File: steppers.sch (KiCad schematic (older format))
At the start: 24 parts, among them J1 HEADER, J10 STEPSTICK, J11 STEPSTICK, J12 STEPSTICK, J2 HEADER, J3 HEADER, J4 STEPSTICK, J5 STEPSTICK, J6 STEPSTICK, J7 HEADER, J8 HEADER, J9 HEADER, P10 CONN_01X04, P11 CONN_01X04, P12 CONN_01X04, P7 CONN_02X04, P8 CONN_01X04, P9 CONN_01X04

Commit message: - added wifi esp8266 - switched caps to smd - fixed dual transistor pinout bug
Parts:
- C12, C13, C14, C15, C16, C17: footprint capacitors:ELCO-8mm-3.5mm_pitch -> capacitors:c_elec_6.3x7.7
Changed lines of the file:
@@
 EESchema Schematic File Version 2
+LIBS:rados-rescue
+LIBS:import-transistors
+LIBS:import-regulators
+LIBS:import-opamps
+LIBS:import-diodes
 LIBS:led_reverse
 LIBS:arduino_shieldsNCL
 LIBS:otheruse_transistors
 LIBS:custom_power
-LIBS:import_resistors
-LIBS:import_regulators
-LIBS:import_transistors
-LIBS:import_diodes
+LIBS:import-misc
+LIBS:armin_misc
 LIBS:power
 LIBS:device
 LIBS:transistors
 LIBS:conn
-LIBS:import_misc
 LIBS:linear
 LIBS:regul
@@
 LIBS:valves
 LIBS:arduino
+LIBS:ESP8266
 LIBS:rados-cache
 EELAYER 25 0
@@
 F 0 "C13" H 3888 1471 50  0000 L CNN
 F 1 "100uF" H 3888 1379 50  0000 L CNN
-F 2 "capacitors:ELCO-8mm-3.5mm_pitch" H 3800 1425 50  0001 C CNN
+F 2 "capacitors:c_elec_6.3x7.7" H 3800 1425 50  0001 C CNN
 F 3 "" H 3800 1425 50  0000 C CNN
 	1    3800 1425
@@
 $EndComp
 $Comp
-L Vsupply #P053
+L Vsupply #P9
 U 1 1 568BEEB3
 P 3150 775
-F 0 "#P053" H 3150 775 60  0001 C CNN
+F 0 "#P9" H 3150 775 60  0001 C CNN
 F 1 "Vsupply" H 3150 725 34  0000 C CNN
 F 2 "" H 3150 775 60  0000 C CNN
@@
 	1150 1125 1150 1425
 $Comp
-L +3.3V #PWR054
+L +3.3V #PWR2
 U 1 1 568BF4F0
 P 1150 1125
-F 0 "#PWR054" H 1150 975 50  0001 C CNN
+F 0 "#PWR2" H 1150 975 50  0001 C CNN
 F 1 "+3.3V" H 1168 1299 50  0000 C CNN
 F 2 "" H 1150 1125 50  0000 C CNN
@@
 $EndComp
 $Comp
-L +3.3V #PWR055
+L +3.3V #PWR29
 U 1 1 568BFD7B
 P 3050 1725
-F 0 "#PWR055" H 3050 1575 50  0001 C CNN
+F 0 "#PWR29" H 3050 1575 50  0001 C CNN
 F 1 "+3.3V" H 3050 1850 50  0000 C CNN
 F 2 "" H 3050 1725 50  0000 C CNN
@@
 	2900 1725 3050 1725
 $Comp
-L GND #PWR056
+L GND #PWR26
 U 1 1 568BFE54
 P 2975 1225
-F 0 "#PWR056" H 2975 975 50  0001 C CNN
+F 0 "#PWR26" H 2975 975 50  0001 C CNN
 F 1 "GND" H 2983 1051 50  0000 C CNN
 F 2 "" H 2975 1225 50  0000 C CNN
@@
 $EndComp
 $Comp
-L GND #PWR057
+L GND #PWR35
 U 1 1 568BFE70
 P 3225 1825
-F 0 "#PWR057" H 3225 1575 50  0001 C CNN
+F 0 "#PWR35" H 3225 1575 50  0001 C CNN
 F 1 "GND" H 3233 1651 50  0000 C CNN
 F 2 "" H 3225 1825 50  0000 C CNN
@@
 F 0 "C14" H 3888 2696 50  0000 L CNN
 F 1 "100uF" H 3888 2604 50  0000 L CNN
-F 2 "capacitors:ELCO-8mm-3.5mm_pitch" H 3800 2650 50  0001 C CNN
+F 2 "capacitors:c_elec_6.3x7.7" H 3800 2650 50  0001 C CNN
 F 3 "" H 3800 2650 50  0000 C CNN
 	1    3800 2650
@@
 $EndComp
 $Comp
-L Vsupply #P058
+L Vsupply #P10
 U 1 1 568BD851
 P 3150 2000
-F 0 "#P058" H 3150 2000 60  0001 C CNN
+F 0 "#P10" H 3150 2000 60  0001 C CNN
 F 1 "Vsupply" H 3150 1950 34  0000 C CNN
 F 2 "" H 3150 2000 60  0000 C CNN
@@
 	1150 2375 1150 2650
 $Comp
-L +3.3V #PWR059
+L +3.3V #PWR3
 U 1 1 568BD862
 P 1150 2375
-F 0 "#PWR059" H 1150 2225 50  0001 C CNN
+F 0 "#PWR3" H 1150 2225 50  0001 C CNN
 F 1 "+3.3V" H 1168 2549 50  0000 C CNN
 F 2 "" H 1150 2375 50  0000 C CNN
@@
 $EndComp
 $Comp
-L +3.3V #PWR060
+L +3.3V #PWR30
 U 1 1 568BD86E
 P 3050 2950
-F 0 "#PWR060" H 3050 2800 50  0001 C CNN
+F 0 "#PWR30" H 3050 2800 50  0001 C CNN
 F 1 "+3.3V" H 3050 3075 50  0000 C CNN
 F 2 "" H 3050 2950 50  0000 C CNN
@@
 	2900 2950 3050 2950
 $Comp
-L GND #PWR061
+L GND #PWR27
 U 1 1 568BD875
 P 2975 2450
-F 0 "#PWR061" H 2975 2200 50  0001 C CNN
+F 0 "#PWR27" H 2975 2200 50  0001 C CNN
 F 1 "GND" H 2983 2276 50  0000 C CNN
 F 2 "" H 2975 2450 50  0000 C CNN
@@
 $EndComp
 $Comp
-L GND #PWR062
+L GND #PWR36
 U 1 1 568BD87B
 P 3225 3050
-F 0 "#PWR062" H 3225 2800 50  0001 C CNN
+F 0 "#PWR36" H 3225 2800 50  0001 C CNN
 F 1 "GND" H 3233 2876 50  0000 C CNN
 F 2 "" H 3225 3050 50  0000 C CNN
@@
 F 0 "C12" H 4038 3996 50  0000 L CNN
 F 1 "100uF" H 4038 3904 50  0000 L CNN
-F 2 "capacitors:ELCO-8mm-3.5mm_pitch" H 3950 3950 50  0001 C CNN
+F 2 "capacitors:c_elec_6.3x7.7" H 3950 3950 50  0001 C CNN
 F 3 "" H 3950 3950 50  0000 C CNN
 	1    3950 3950
@@
 $EndComp
 $Comp
-L Vsupply #P063
+L Vsupply #P8
 U 1 1 568BDFCA
 P 3125 3300
-F 0 "#P063" H 3125 3300 60  0001 C CNN
+F 0 "#P8" H 3125 3300 60  0001 C CNN
 F 1 "Vsupply" H 3125 3250 34  0000 C CNN
 F 2 "" H 3125 3300 60  0000 C CNN
@@
 	1125 3650 1125 3950
 $Comp
-L +3.3V #PWR064
+L +3.3V #PWR1
 U 1 1 568BDFDB
 P 1125 3650
-F 0 "#PWR064" H 1125 3500 50  0001 C CNN
+F 0 "#PWR1" H 1125 3500 50  0001 C CNN
 F 1 "+3.3V" H 1143 3824 50  0000 C CNN
 F 2 "" H 1125 3650 50  0000 C CNN
@@
 $EndComp
 $Comp
-L +3.3V #PWR065
+L +3.3V #PWR28
 U 1 1 568BDFE7
 P 3025 4250
-F 0 "#PWR065" H 3025 4100 50  0001 C CNN
+F 0 "#PWR28" H 3025 4100 50  0001 C CNN
 F 1 "+3.3V" H 3025 4375 50  0000 C CNN
 F 2 "" H 3025 4250 50  0000 C CNN
@@
 	2875 4250 3025 4250
 $Comp
-L GND #PWR066
+L GND #PWR25
 U 1 1 568BDFEE
 P 2950 3750
-F 0 "#PWR066" H 2950 3500 50  0001 C CNN
+F 0 "#PWR25" H 2950 3500 50  0001 C CNN
 F 1 "GND" H 2958 3576 50  0000 C CNN
 F 2 "" H 2950 3750 50  0000 C CNN
@@
 $EndComp
 $Comp
-L GND #PWR067
+L GND #PWR34
 U 1 1 568BDFF4
 P 3200 4350
-F 0 "#PWR067" H 3200 4100 50  0001 C CNN
+F 0 "#PWR34" H 3200 4100 50  0001 C CNN
 F 1 "GND" H 3208 4176 50  0000 C CNN
 F 2 "" H 3200 4350 50  0000 C CNN
@@
 F 0 "C15" H 8988 4121 50  0000 L CNN
 F 1 "100uF" H 8988 4029 50  0000 L CNN
-F 2 "capacitors:ELCO-8mm-3.5mm_pitch" H 8900 4075 50  0001 C CNN
+F 2 "capacitors:c_elec_6.3x7.7" H 8900 4075 50  0001 C CNN
 F 3 "" H 8900 4075 50  0000 C CNN
 	1    8900 4075
@@
 $EndComp
 $Comp
-L Vsupply #P068
+L Vsupply #P20
 U 1 1 568C39F8
 P 8250 3425
-F 0 "#P068" H 8250 3425 60  0001 C CNN
+F 0 "#P20" H 8250 3425 60  0001 C CNN
 F 1 "Vsupply" H 8250 3375 34  0000 C CNN
 F 2 "" H 8250 3425 60  0000 C CNN
@@
 	6250 4075 6250 3775
 $Comp
-L +3.3V #PWR069
+L +3.3V #PWR56
 U 1 1 568C3A09
 P 6250 3775
-F 0 "#PWR069" H 6250 3625 50  0001 C CNN
+F 0 "#PWR56" H 6250 3625 50  0001 C CNN
 F 1 "+3.3V" H 6268 3949 50  0000 C CNN
 F 2 "" H 6250 3775 50  0000 C CNN
@@
 $EndComp
 $Comp
-L +3.3V #PWR070
+L +3.3V #PWR72
 U 1 1 568C3A15
 P 8150 4375
-F 0 "#PWR070" H 8150 4225 50  0001 C CNN
+F 0 "#PWR72" H 8150 4225 50  0001 C CNN
 F 1 "+3.3V" H 8150 4500 50  0000 C CNN
 F 2 "" H 8150 4375 50  0000 C CNN
@@
 	8000 4375 8150 4375
 $Comp
-L GND #PWR071
+L GND #PWR69
 U 1 1 568C3A1C
 P 8075 3875
-F 0 "#PWR071" H 8075 3625 50  0001 C CNN
+F 0 "#PWR69" H 8075 3625 50  0001 C CNN
 F 1 "GND" H 8083 3701 50  0000 C CNN
 F 2 "" H 8075 3875 50  0000 C CNN
@@
 $EndComp
 $Comp
-L GND #PWR072
+L GND #PWR75
 U 1 1 568C3A22
 P 8325 4475
-F 0 "#PWR072" H 8325 4225 50  0001 C CNN
+F 0 "#PWR75" H 8325 4225 50  0001 C CNN
 F 1 "GND" H 8333 4301 50  0000 C CNN
 F 2 "" H 8325 4475 50  0000 C CNN
@@
 F 0 "C16" H 8963 1446 50  0000 L CNN
 F 1 "100uF" H 8963 1354 50  0000 L CNN
-F 2 "capacitors:ELCO-8mm-3.5mm_pitch" H 8875 1400 50  0001 C CNN
+F 2 "capacitors:c_elec_6.3x7.7" H 8875 1400 50  0001 C CNN
 F 3 "" H 8875 1400 50  0000 C CNN
 	1    8875 1400
@@
 $EndComp
 $Comp
-L Vsupply #P073
+L Vsupply #P18
 U 1 1 568C3E5C
 P 8225 750
-F 0 "#P073" H 8225 750 60  0001 C CNN
+F 0 "#P18" H 8225 750 60  0001 C CNN
 F 1 "Vsupply" H 8225 700 34  0000 C CNN
 F 2 "" H 8225 750 60  0000 C CNN
@@
 	6225 1100 6225 1400
 $Comp
-L +3.3V #PWR074
+L +3.3V #PWR54
 U 1 1 568C3E6D
 P 6225 1100
-F 0 "#PWR074" H 6225 950 50  0001 C CNN
+F 0 "#PWR54" H 6225 950 50  0001 C CNN
 F 1 "+3.3V" H 6243 1274 50  0000 C CNN
 F 2 "" H 6225 1100 50  0000 C CNN
@@
 $EndComp
 $Comp
-L +3.3V #PWR075
+L +3.3V #PWR70
 U 1 1 568C3E79
 P 8125 1700
-F 0 "#PWR075" H 8125 1550 50  0001 C CNN
+F 0 "#PWR70" H 8125 1550 50  0001 C CNN
 F 1 "+3.3V" H 8125 1825 50  0000 C CNN
 F 2 "" H 8125 1700 50  0000 C CNN
@@
 	7975 1700 8125 1700
 $Comp
-L GND #PWR076
+L GND #PWR67
 U 1 1 568C3E80
 P 8050 1200
-F 0 "#PWR076" H 8050 950 50  0001 C CNN
+F 0 "#PWR67" H 8050 950 50  0001 C CNN
 F 1 "GND" H 8058 1026 50  0000 C CNN
 F 2 "" H 8050 1200 50  0000 C CNN
@@
 $EndComp
 $Comp
-L GND #PWR077
+L GND #PWR73
 U 1 1 568C3E86
 P 8300 1800
-F 0 "#PWR077" H 8300 1550 50  0001 C CNN
+F 0 "#PWR73" H 8300 1550 50  0001 C CNN
 F 1 "GND" H 8308 1626 50  0000 C CNN
 F 2 "" H 8300 1800 50  0000 C CNN
@@
 F 0 "C17" H 8963 2821 50  0000 L CNN
 F 1 "100uF" H 8963 2729 50  0000 L CNN
-F 2 "capacitors:ELCO-8mm-3.5mm_pitch" H 8875 2775 50  0001 C CNN
+F 2 "capacitors:c_elec_6.3x7.7" H 8875 2775 50  0001 C CNN
 F 3 "" H 8875 2775 50  0000 C CNN
 	1    8875 2775
@@
 $EndComp
 $Comp
-L Vsupply #P078
+L Vsupply #P19
 U 1 1 568C4325
 P 8225 2125
-F 0 "#P078" H 8225 2125 60  0001 C CNN
+F 0 "#P19" H 8225 2125 60  0001 C CNN
 F 1 "Vsupply" H 8225 2075 34  0000 C CNN
 F 2 "" H 8225 2125 60  0000 C CNN
@@
 	6225 2475 6225 2775
 $Comp
-L +3.3V #PWR079
+L +3.3V #PWR55
 U 1 1 568C4336
 P 6225 2475
-F 0 "#PWR079" H 6225 2325 50  0001 C CNN
+F 0 "#PWR55" H 6225 2325 50  0001 C CNN
 F 1 "+3.3V" H 6243 2649 50  0000 C CNN
 F 2 "" H 6225 2475 50  0000 C CNN
@@
 $EndComp
 $Comp
-L +3.3V #PWR080
+L +3.3V #PWR71
 U 1 1 568C4342
 P 8125 3075
-F 0 "#PWR080" H 8125 2925 50  0001 C CNN
+F 0 "#PWR71" H 8125 2925 50  0001 C CNN
 F 1 "+3.3V" H 8125 3200 50  0000 C CNN
 F 2 "" H 8125 3075 50  0000 C CNN
@@
 	7975 3075 8125 3075
 $Comp
-L GND #PWR081
+L GND #PWR68
 U 1 1 568C4349
 P 8050 2575
-F 0 "#PWR081" H 8050 2325 50  0001 C CNN
+F 0 "#PWR68" H 8050 2325 50  0001 C CNN
 F 1 "GND" H 8058 2401 50  0000 C CNN
 F 2 "" H 8050 2575 50  0000 C CNN
@@
 $EndComp
 $Comp
-L GND #PWR082
+L GND #PWR74
 U 1 1 568C434F
 P 8300 3175
-F 0 "#PWR082" H 8300 2925 50  0001 C CNN
+F 0 "#PWR74" H 8300 2925 50  0001 C CNN
 F 1 "GND" H 8308 3001 50  0000 C CNN
 F 2 "" H 8300 3175 50  0000 C CNN

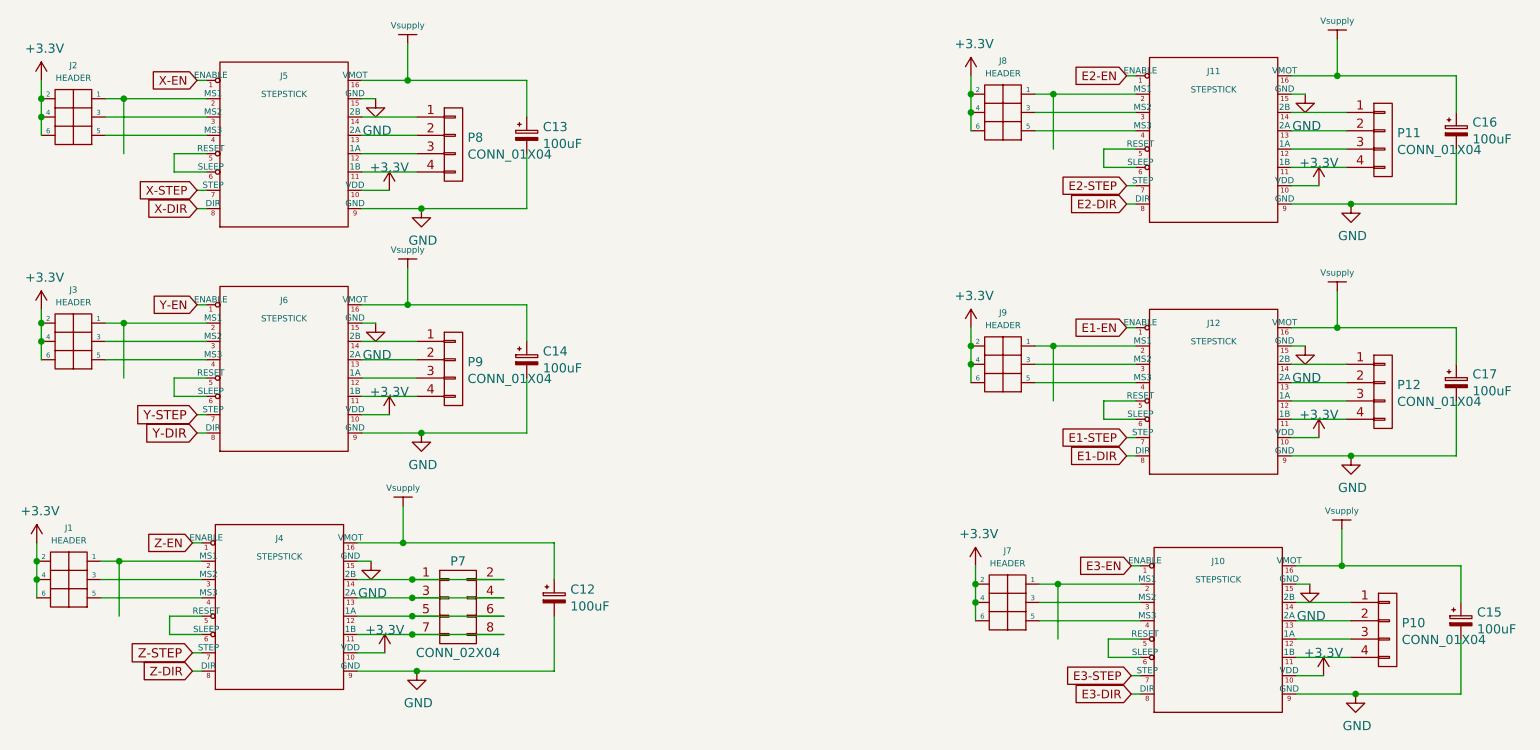
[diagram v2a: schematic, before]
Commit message: Added minimal arduino mega support
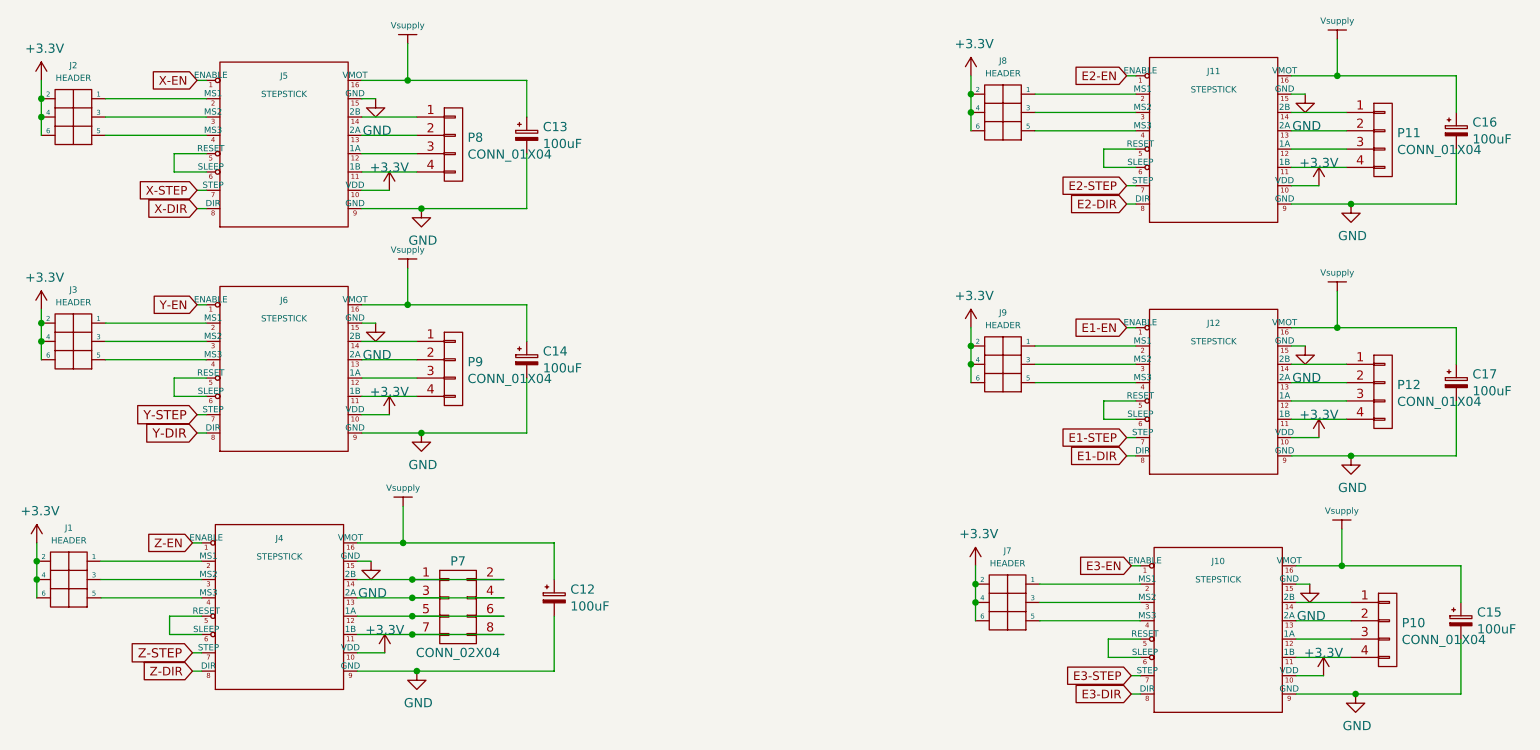
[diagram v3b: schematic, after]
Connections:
- wire segments 132 -> 126
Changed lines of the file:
@@
 	2900 1125 3800 1125
 Connection ~ 3150 1125
-Wire Wire Line
-	1600 1225 1600 1525
-Connection ~ 1600 1225
 Text GLabel 2000 1125 0    47   Input ~ 0
 X-EN
@@
 $EndComp
 $Comp
-L Vsupply #P18
+L Vsupply #P19
 U 1 1 568BEEB3
 P 3150 775
-F 0 "#P18" H 3150 775 60  0001 C CNN
+F 0 "#P19" H 3150 775 60  0001 C CNN
 F 1 "Vsupply" H 3150 725 34  0000 C CNN
 F 2 "" H 3150 775 60  0000 C CNN
@@
 	1150 1125 1150 1425
 $Comp
-L +3.3V #PWR42
+L +3.3V #PWR43
 U 1 1 568BF4F0
 P 1150 1125
-F 0 "#PWR42" H 1150 975 50  0001 C CNN
+F 0 "#PWR43" H 1150 975 50  0001 C CNN
 F 1 "+3.3V" H 1168 1299 50  0000 C CNN
 F 2 "" H 1150 1125 50  0000 C CNN
@@
 $EndComp
 $Comp
-L +3.3V #PWR48
+L +3.3V #PWR49
 U 1 1 568BFD7B
 P 3050 1725
-F 0 "#PWR48" H 3050 1575 50  0001 C CNN
+F 0 "#PWR49" H 3050 1575 50  0001 C CNN
 F 1 "+3.3V" H 3050 1850 50  0000 C CNN
 F 2 "" H 3050 1725 50  0000 C CNN
@@
 	2900 1725 3050 1725
 $Comp
-L GND #PWR45
+L GND #PWR46
 U 1 1 568BFE54
 P 2975 1225
-F 0 "#PWR45" H 2975 975 50  0001 C CNN
+F 0 "#PWR46" H 2975 975 50  0001 C CNN
 F 1 "GND" H 2983 1051 50  0000 C CNN
 F 2 "" H 2975 1225 50  0000 C CNN
@@
 $EndComp
 $Comp
-L GND #PWR51
+L GND #PWR52
 U 1 1 568BFE70
 P 3225 1825
-F 0 "#PWR51" H 3225 1575 50  0001 C CNN
+F 0 "#PWR52" H 3225 1575 50  0001 C CNN
 F 1 "GND" H 3233 1651 50  0000 C CNN
 F 2 "" H 3225 1825 50  0000 C CNN
@@
 $EndComp
 $Comp
-L Vsupply #P19
+L Vsupply #P20
 U 1 1 568BD851
 P 3150 2000
-F 0 "#P19" H 3150 2000 60  0001 C CNN
+F 0 "#P20" H 3150 2000 60  0001 C CNN
 F 1 "Vsupply" H 3150 1950 34  0000 C CNN
 F 2 "" H 3150 2000 60  0000 C CNN
@@
 	1150 2375 1150 2650
 $Comp
-L +3.3V #PWR43
+L +3.3V #PWR44
 U 1 1 568BD862
 P 1150 2375
-F 0 "#PWR43" H 1150 2225 50  0001 C CNN
+F 0 "#PWR44" H 1150 2225 50  0001 C CNN
 F 1 "+3.3V" H 1168 2549 50  0000 C CNN
 F 2 "" H 1150 2375 50  0000 C CNN
@@
 $EndComp
 $Comp
-L +3.3V #PWR49
+L +3.3V #PWR50
 U 1 1 568BD86E
 P 3050 2950
-F 0 "#PWR49" H 3050 2800 50  0001 C CNN
+F 0 "#PWR50" H 3050 2800 50  0001 C CNN
 F 1 "+3.3V" H 3050 3075 50  0000 C CNN
 F 2 "" H 3050 2950 50  0000 C CNN
@@
 	2900 2950 3050 2950
 $Comp
-L GND #PWR46
+L GND #PWR47
 U 1 1 568BD875
 P 2975 2450
-F 0 "#PWR46" H 2975 2200 50  0001 C CNN
+F 0 "#PWR47" H 2975 2200 50  0001 C CNN
 F 1 "GND" H 2983 2276 50  0000 C CNN
 F 2 "" H 2975 2450 50  0000 C CNN
@@
 $EndComp
 $Comp
-L GND #PWR52
+L GND #PWR53
 U 1 1 568BD87B
 P 3225 3050
-F 0 "#PWR52" H 3225 2800 50  0001 C CNN
+F 0 "#PWR53" H 3225 2800 50  0001 C CNN
 F 1 "GND" H 3233 2876 50  0000 C CNN
 F 2 "" H 3225 3050 50  0000 C CNN
@@
 	2875 3650 3950 3650
 Connection ~ 3125 3650
-Wire Wire Line
-	1575 3750 1575 4050
-Connection ~ 1575 3750
 Text GLabel 1975 3650 0    47   Input ~ 0
 Z-EN
@@
 $EndComp
 $Comp
-L Vsupply #P17
+L Vsupply #P18
 U 1 1 568BDFCA
 P 3125 3300
-F 0 "#P17" H 3125 3300 60  0001 C CNN
+F 0 "#P18" H 3125 3300 60  0001 C CNN
 F 1 "Vsupply" H 3125 3250 34  0000 C CNN
 F 2 "" H 3125 3300 60  0000 C CNN
@@
 	1125 3650 1125 3950
 $Comp
-L +3.3V #PWR41
+L +3.3V #PWR42
 U 1 1 568BDFDB
 P 1125 3650
-F 0 "#PWR41" H 1125 3500 50  0001 C CNN
+F 0 "#PWR42" H 1125 3500 50  0001 C CNN
 F 1 "+3.3V" H 1143 3824 50  0000 C CNN
 F 2 "" H 1125 3650 50  0000 C CNN
@@
 $EndComp
 $Comp
-L +3.3V #PWR47
+L +3.3V #PWR48
 U 1 1 568BDFE7
 P 3025 4250
-F 0 "#PWR47" H 3025 4100 50  0001 C CNN
+F 0 "#PWR48" H 3025 4100 50  0001 C CNN
 F 1 "+3.3V" H 3025 4375 50  0000 C CNN
 F 2 "" H 3025 4250 50  0000 C CNN
@@
 	2875 4250 3025 4250
 $Comp
-L GND #PWR44
+L GND #PWR45
 U 1 1 568BDFEE
 P 2950 3750
-F 0 "#PWR44" H 2950 3500 50  0001 C CNN
+F 0 "#PWR45" H 2950 3500 50  0001 C CNN
 F 1 "GND" H 2958 3576 50  0000 C CNN
 F 2 "" H 2950 3750 50  0000 C CNN
@@
 $EndComp
 $Comp
-L GND #PWR50
+L GND #PWR51
 U 1 1 568BDFF4
 P 3200 4350
-F 0 "#PWR50" H 3200 4100 50  0001 C CNN
+F 0 "#PWR51" H 3200 4100 50  0001 C CNN
 F 1 "GND" H 3208 4176 50  0000 C CNN
 F 2 "" H 3200 4350 50  0000 C CNN
@@
 	8000 3775 8900 3775
 Connection ~ 8250 3775
-Wire Wire Line
-	6700 3875 6700 4175
-Connection ~ 6700 3875
 Text GLabel 7100 3775 0    47   Input ~ 0
 E3-EN
@@
 $EndComp
 $Comp
-L Vsupply #P22
+L Vsupply #P23
 U 1 1 568C39F8
 P 8250 3425
-F 0 "#P22" H 8250 3425 60  0001 C CNN
+F 0 "#P23" H 8250 3425 60  0001 C CNN
 F 1 "Vsupply" H 8250 3375 34  0000 C CNN
 F 2 "" H 8250 3425 60  0000 C CNN
@@
 	6250 4075 6250 3775
 $Comp
-L +3.3V #PWR55
+L +3.3V #PWR56
 U 1 1 568C3A09
 P 6250 3775
-F 0 "#PWR55" H 6250 3625 50  0001 C CNN
+F 0 "#PWR56" H 6250 3625 50  0001 C CNN
 F 1 "+3.3V" H 6268 3949 50  0000 C CNN
 F 2 "" H 6250 3775 50  0000 C CNN
@@
 $EndComp
 $Comp
-L +3.3V #PWR61
+L +3.3V #PWR62
 U 1 1 568C3A15
 P 8150 4375
-F 0 "#PWR61" H 8150 4225 50  0001 C CNN
+F 0 "#PWR62" H 8150 4225 50  0001 C CNN
 F 1 "+3.3V" H 8150 4500 50  0000 C CNN
 F 2 "" H 8150 4375 50  0000 C CNN
@@
 	8000 4375 8150 4375
 $Comp
-L GND #PWR58
+L GND #PWR59
 U 1 1 568C3A1C
 P 8075 3875
-F 0 "#PWR58" H 8075 3625 50  0001 C CNN
+F 0 "#PWR59" H 8075 3625 50  0001 C CNN
 F 1 "GND" H 8083 3701 50  0000 C CNN
 F 2 "" H 8075 3875 50  0000 C CNN
@@
 $EndComp
 $Comp
-L GND #PWR64
+L GND #PWR65
 U 1 1 568C3A22
 P 8325 4475
-F 0 "#PWR64" H 8325 4225 50  0001 C CNN
+F 0 "#PWR65" H 8325 4225 50  0001 C CNN
 F 1 "GND" H 8333 4301 50  0000 C CNN
 F 2 "" H 8325 4475 50  0000 C CNN
@@
 	7975 1100 8875 1100
 Connection ~ 8225 1100
-Wire Wire Line
-	6675 1200 6675 1500
-Connection ~ 6675 1200
 Text GLabel 7075 2475 0    47   Input ~ 0
 E1-EN
@@
 $EndComp
 $Comp
-L Vsupply #P20
+L Vsupply #P21
 U 1 1 568C3E5C
 P 8225 750
-F 0 "#P20" H 8225 750 60  0001 C CNN
+F 0 "#P21" H 8225 750 60  0001 C CNN
 F 1 "Vsupply" H 8225 700 34  0000 C CNN
 F 2 "" H 8225 750 60  0000 C CNN
@@
 	6225 1100 6225 1400
 $Comp
-L +3.3V #PWR53
+L +3.3V #PWR54
 U 1 1 568C3E6D
 P 6225 1100
-F 0 "#PWR53" H 6225 950 50  0001 C CNN
+F 0 "#PWR54" H 6225 950 50  0001 C CNN
 F 1 "+3.3V" H 6243 1274 50  0000 C CNN
 F 2 "" H 6225 1100 50  0000 C CNN
@@
 $EndComp
 $Comp
-L +3.3V #PWR59
+L +3.3V #PWR60
 U 1 1 568C3E79
 P 8125 1700
-F 0 "#PWR59" H 8125 1550 50  0001 C CNN
+F 0 "#PWR60" H 8125 1550 50  0001 C CNN
 F 1 "+3.3V" H 8125 1825 50  0000 C CNN
 F 2 "" H 8125 1700 50  0000 C CNN
@@
 	7975 1700 8125 1700
 $Comp
-L GND #PWR56
+L GND #PWR57
 U 1 1 568C3E80
 P 8050 1200
-F 0 "#PWR56" H 8050 950 50  0001 C CNN
+F 0 "#PWR57" H 8050 950 50  0001 C CNN
 F 1 "GND" H 8058 1026 50  0000 C CNN
 F 2 "" H 8050 1200 50  0000 C CNN
@@
 $EndComp
 $Comp
-L GND #PWR62
+L GND #PWR63
 U 1 1 568C3E86
 P 8300 1800
-F 0 "#PWR62" H 8300 1550 50  0001 C CNN
+F 0 "#PWR63" H 8300 1550 50  0001 C CNN
 F 1 "GND" H 8308 1626 50  0000 C CNN
 F 2 "" H 8300 1800 50  0000 C CNN
@@
 	7975 2475 8875 2475
 Connection ~ 8225 2475
-Wire Wire Line
-	6675 2575 6675 2875
-Connection ~ 6675 2575
 Text GLabel 7075 1100 0    47   Input ~ 0
 E2-EN
@@
 $EndComp
 $Comp
-L Vsupply #P21
+L Vsupply #P22
 U 1 1 568C4325
 P 8225 2125
-F 0 "#P21" H 8225 2125 60  0001 C CNN
+F 0 "#P22" H 8225 2125 60  0001 C CNN
 F 1 "Vsupply" H 8225 2075 34  0000 C CNN
 F 2 "" H 8225 2125 60  0000 C CNN
@@
 	6225 2475 6225 2775
 $Comp
-L +3.3V #PWR54
+L +3.3V #PWR55
 U 1 1 568C4336
 P 6225 2475
-F 0 "#PWR54" H 6225 2325 50  0001 C CNN
+F 0 "#PWR55" H 6225 2325 50  0001 C CNN
 F 1 "+3.3V" H 6243 2649 50  0000 C CNN
 F 2 "" H 6225 2475 50  0000 C CNN
@@
 $EndComp
 $Comp
-L +3.3V #PWR60
+L +3.3V #PWR61
 U 1 1 568C4342
 P 8125 3075
-F 0 "#PWR60" H 8125 2925 50  0001 C CNN
+F 0 "#PWR61" H 8125 2925 50  0001 C CNN
 F 1 "+3.3V" H 8125 3200 50  0000 C CNN
 F 2 "" H 8125 3075 50  0000 C CNN
@@
 	7975 3075 8125 3075
 $Comp
-L GND #PWR57
+L GND #PWR58
 U 1 1 568C4349
 P 8050 2575
-F 0 "#PWR57" H 8050 2325 50  0001 C CNN
+F 0 "#PWR58" H 8050 2325 50  0001 C CNN
 F 1 "GND" H 8058 2401 50  0000 C CNN
 F 2 "" H 8050 2575 50  0000 C CNN
@@
 $EndComp
 $Comp
-L GND #PWR63
+L GND #PWR64
 U 1 1 568C434F
 P 8300 3175
-F 0 "#PWR63" H 8300 2925 50  0001 C CNN
+F 0 "#PWR64" H 8300 2925 50  0001 C CNN
 F 1 "GND" H 8308 3001 50  0000 C CNN
 F 2 "" H 8300 3175 50  0000 C CNN
@@
 Connection ~ 1150 2450
 Connection ~ 1150 2550
-Connection ~ 1600 2450
-Wire Wire Line
-	1600 2450 1600 2750
 Connection ~ 1150 1225
 Connection ~ 1150 1325
